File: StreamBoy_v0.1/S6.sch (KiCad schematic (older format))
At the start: 24 parts, among them U1 XC6SLX9-TQG144

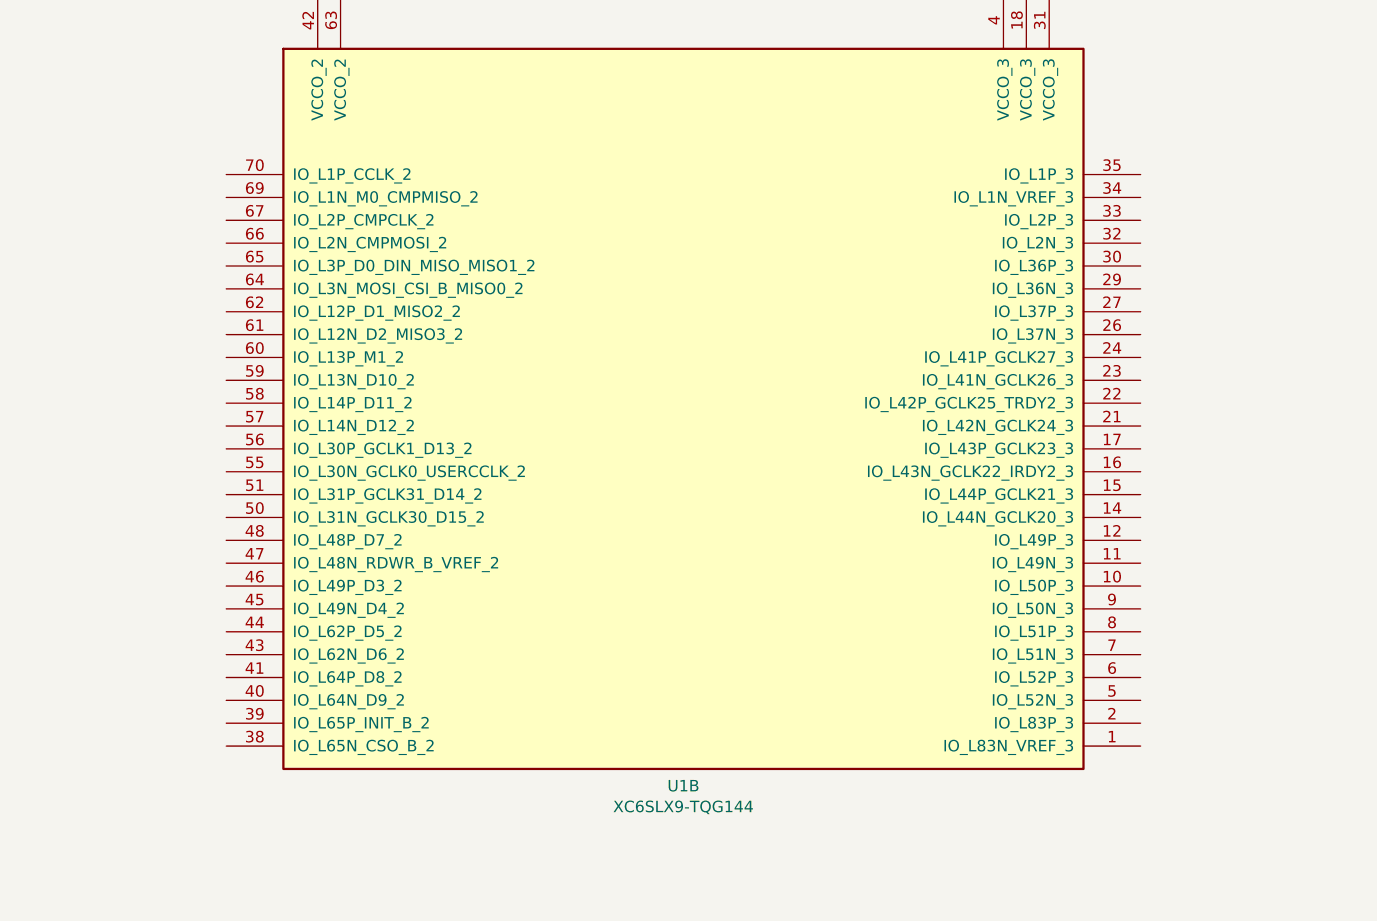
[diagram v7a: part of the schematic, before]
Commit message: Replace reset button with a jumper
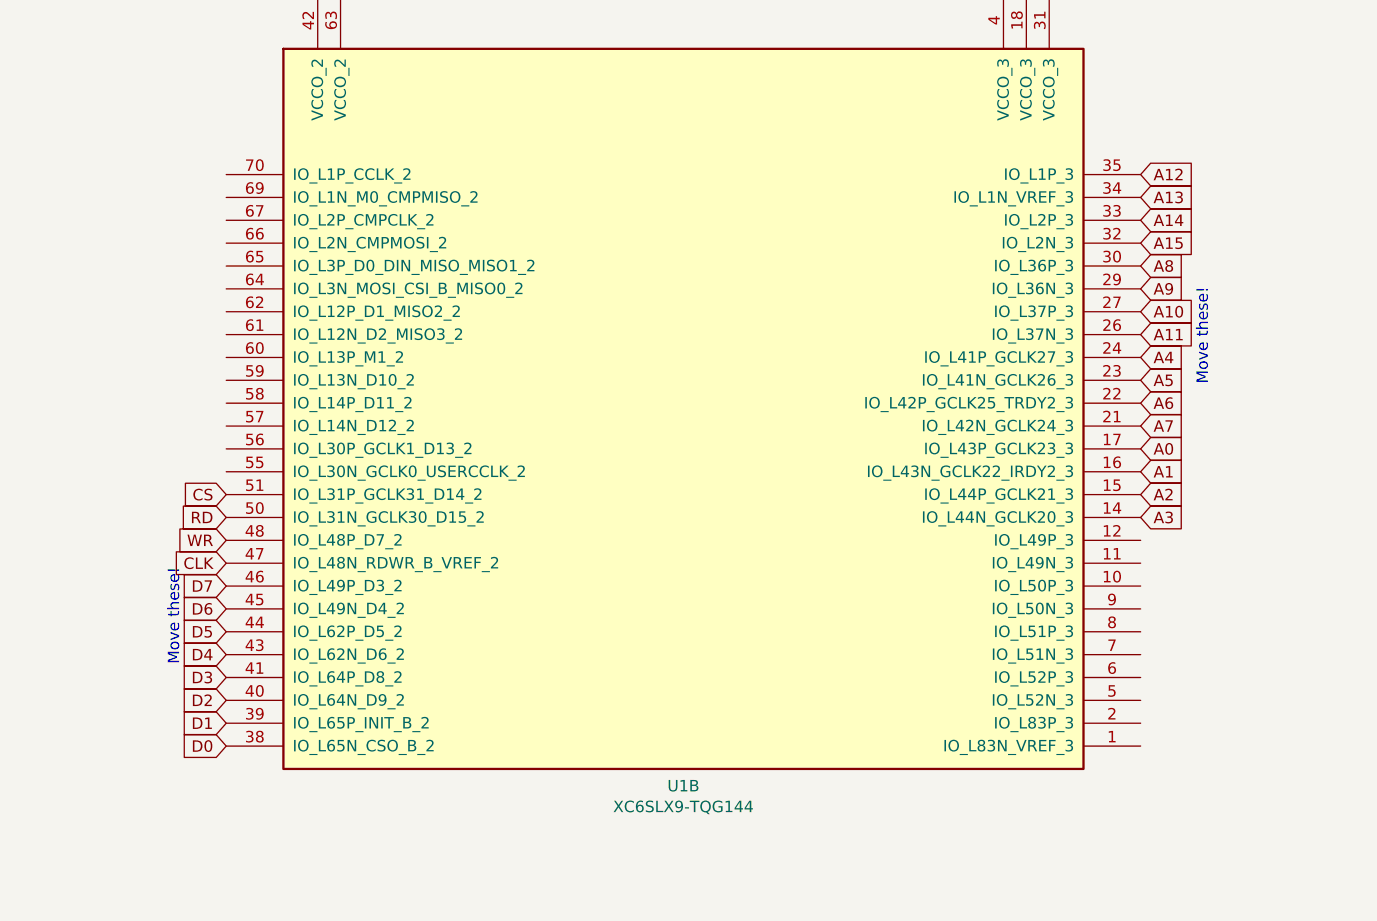
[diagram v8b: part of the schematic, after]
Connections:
- net A3: now reaches U1.14 (IO_L44N_GCLK20_3)
- net A2: now reaches U1.15 (IO_L44P_GCLK21_3)
- net A1: now reaches U1.16 (IO_L43N_GCLK22_IRDY2_3)
- net A0: now reaches U1.17 (IO_L43P_GCLK23_3)
- net A7: now reaches U1.21 (IO_L42N_GCLK24_3)
- net A6: now reaches U1.22 (IO_L42P_GCLK25_TRDY2_3)
- net A5: now reaches U1.23 (IO_L41N_GCLK26_3)
- net A4: now reaches U1.24 (IO_L41P_GCLK27_3)
- net A11: now reaches U1.26 (IO_L37N_3)
- net A10: now reaches U1.27 (IO_L37P_3)
- net A9: now reaches U1.29 (IO_L36N_3)
- net A8: now reaches U1.30 (IO_L36P_3)
- net A15: now reaches U1.32 (IO_L2N_3)
- net A14: now reaches U1.33 (IO_L2P_3)
- net A13: now reaches U1.34 (IO_L1N_VREF_3)
- net A12: now reaches U1.35 (IO_L1P_3)
- net D0: now reaches U1.38 (IO_L65N_CSO_B_2)
- net D1: now reaches U1.39 (IO_L65P_INIT_B_2)
- net D2: now reaches U1.40 (IO_L64N_D9_2)
- net D3: now reaches U1.41 (IO_L64P_D8_2)
- net D4: now reaches U1.43 (IO_L62N_D6_2)
- net D5: now reaches U1.44 (IO_L62P_D5_2)
- net D6: now reaches U1.45 (IO_L49N_D4_2)
- net D7: now reaches U1.46 (IO_L49P_D3_2)
- net CLK: now reaches U1.47 (IO_L48N_RDWR_B_VREF_2)
- net WR: now reaches U1.48 (IO_L48P_D7_2)
- net RD: now reaches U1.50 (IO_L31N_GCLK30_D15_2)
- net CS: now reaches U1.51 (IO_L31P_GCLK31_D14_2)
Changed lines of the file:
@@
 Text Notes 6500 3350 0    50   ~ 0
 Move these!
+Text GLabel 13700 3050 2    50   Input ~ 0
+A0
+Text GLabel 13700 3150 2    50   Input ~ 0
+A1
+Text GLabel 13700 3250 2    50   Input ~ 0
+A2
+Text GLabel 13700 3350 2    50   Input ~ 0
+A3
+Text GLabel 13700 2650 2    50   Input ~ 0
+A4
+Text GLabel 13700 2750 2    50   Input ~ 0
+A5
+Text GLabel 13700 2850 2    50   Input ~ 0
+A6
+Text GLabel 13700 2950 2    50   Input ~ 0
+A7
+Text GLabel 13700 2250 2    50   Input ~ 0
+A8
+Text GLabel 13700 2350 2    50   Input ~ 0
+A9
+Text GLabel 13700 2450 2    50   Input ~ 0
+A10
+Text GLabel 13700 2550 2    50   Input ~ 0
+A11
+Text GLabel 13700 1850 2    50   Input ~ 0
+A12
+Text GLabel 13700 1950 2    50   Input ~ 0
+A13
+Text GLabel 13700 2050 2    50   Input ~ 0
+A14
+Text GLabel 13700 2150 2    50   Input ~ 0
+A15
+Text GLabel 9700 3550 0    50   Input ~ 0
+CLK
+Text GLabel 9700 3450 0    50   Input ~ 0
+WR
+Text GLabel 9700 3350 0    50   Input ~ 0
+RD
+Text GLabel 9700 3250 0    50   Input ~ 0
+CS
+Text GLabel 9700 3650 0    50   Input ~ 0
+D7
+Text GLabel 9700 3750 0    50   Input ~ 0
+D6
+Text GLabel 9700 3850 0    50   Input ~ 0
+D5
+Text GLabel 9700 3950 0    50   Input ~ 0
+D4
+Text GLabel 9700 4350 0    50   Input ~ 0
+D0
+Text GLabel 9700 4250 0    50   Input ~ 0
+D1
+Text GLabel 9700 4150 0    50   Input ~ 0
+D2
+Text GLabel 9700 4050 0    50   Input ~ 0
+D3
+Text Notes 9500 4000 1    50   ~ 0
+Move these!
+Text Notes 14000 2350 3    50   ~ 0
+Move these!
 $EndSCHEMATC
